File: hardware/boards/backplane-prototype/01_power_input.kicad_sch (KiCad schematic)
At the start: 42 parts, among them J5 DC INPUT (GND / +VIN), U2 LM5164DDAR, U3 LM5164DDAR, U4 INA237AIDGSR

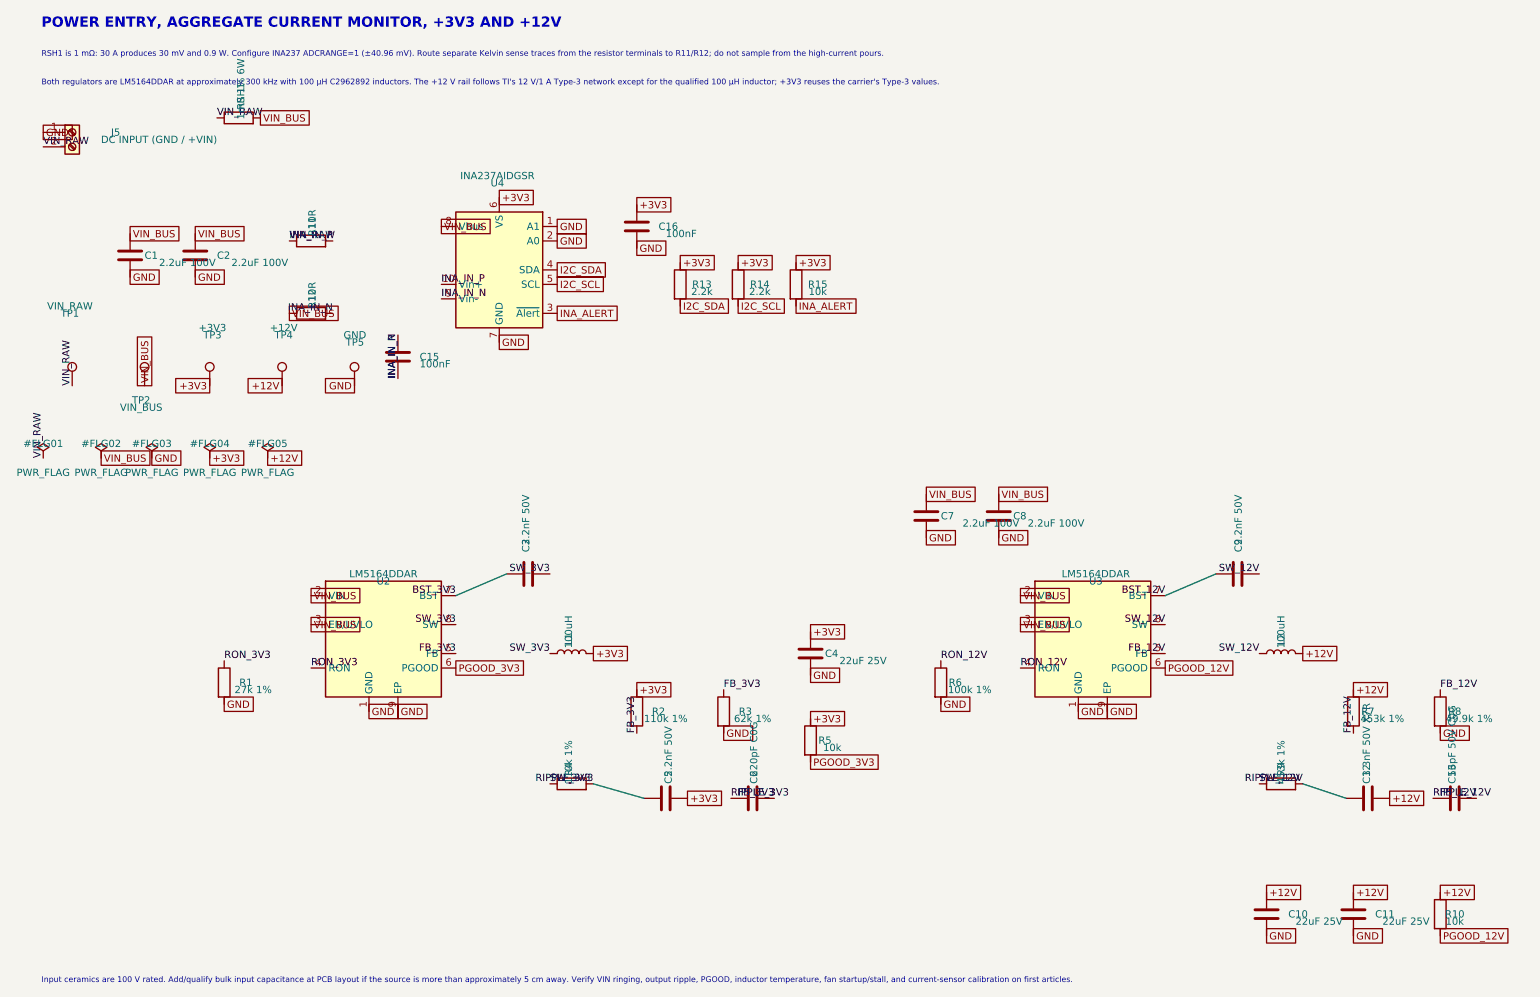
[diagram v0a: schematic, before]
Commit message: checkpoint backplane PCB synchronization
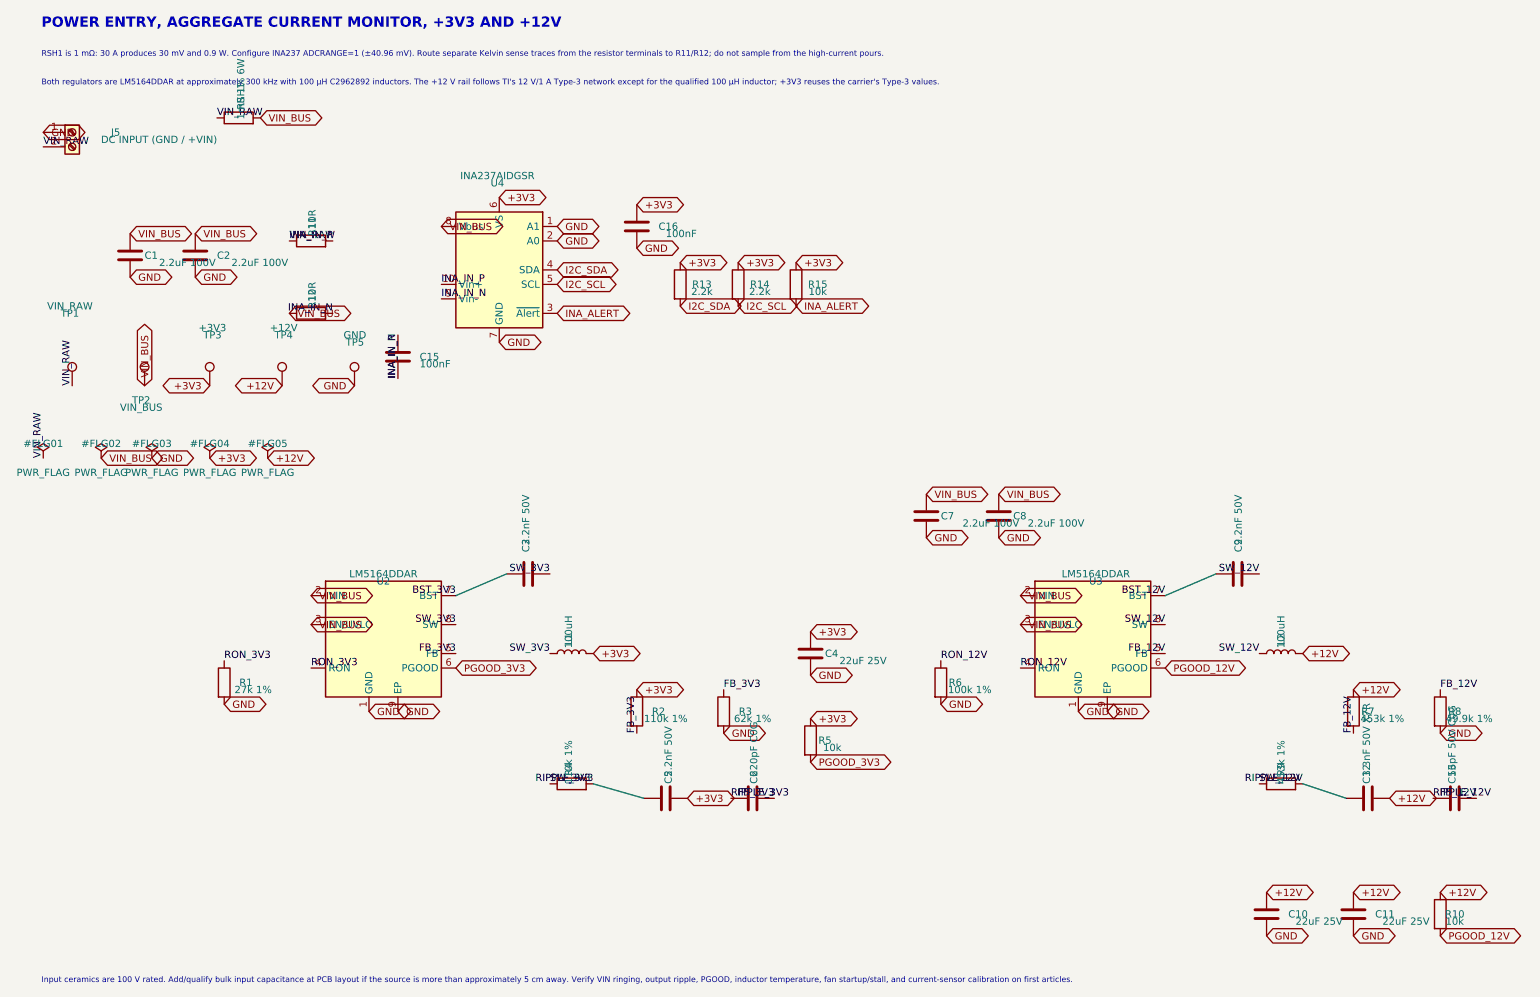
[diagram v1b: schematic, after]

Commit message: hardware: mark all test points DNP
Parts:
- TP1, TP2, TP3, TP4, TP5: now not fitted; now left out of the parts list
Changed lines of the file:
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@@
 		(body_style 1)
 		(exclude_from_sim no)
-		(in_bom yes)
+		(in_bom no)
 		(on_board yes)
 		(in_pos_files yes)
-		(dnp no)
+		(dnp yes)
 		(property "Reference" "TP2"
 			(at 37.5 82.55 0)
@@
 		(body_style 1)
 		(exclude_from_sim no)
-		(in_bom yes)
+		(in_bom no)
 		(on_board yes)
 		(in_pos_files yes)
-		(dnp no)
+		(dnp yes)
 		(property "Reference" "TP5"
 			(at 75 72.39 0)
@@
 		(body_style 1)
 		(exclude_from_sim no)
-		(in_bom yes)
+		(in_bom no)
 		(on_board yes)
 		(in_pos_files yes)
-		(dnp no)
+		(dnp yes)
 		(property "Reference" "TP1"
 			(at 25 67.31 0)
@@
 		(body_style 1)
 		(exclude_from_sim no)
-		(in_bom yes)
+		(in_bom no)
 		(on_board yes)
 		(in_pos_files yes)
-		(dnp no)
+		(dnp yes)
 		(property "Reference" "TP4"
 			(at 62.5 71.12 0)
@@
 		(body_style 1)
 		(exclude_from_sim no)
-		(in_bom yes)
+		(in_bom no)
 		(on_board yes)
 		(in_pos_files yes)
-		(dnp no)
+		(dnp yes)
 		(property "Reference" "TP3"
 			(at 50 71.12 0)

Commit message: hardware: remove unused 3v3 power-good pull-up
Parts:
- removed R5: 10k, Resistor_SMD:R_0603_1608Metric, symbol Device:R
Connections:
- net PGOOD_3V3: no longer names the net of U2.6 (PGOOD)
- no-connect marks 0 -> 1
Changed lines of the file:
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@@
 		)
 	)
-	(global_label "PGOOD_3V3"
-		(shape bidirectional)
-		(at 154.94 146.05 0)
-		(effects
-			(font
-				(size 1.27 1.27)
-			)
-			(justify left)
-		)
-		(property "Intersheetrefs" "${INTERSHEET_REFS}"
-			(at 154.94 146.05 0)
-			(hide yes)
-			(show_name no)
-			(do_not_autoplace no)
-			(effects
-				(font
-					(size 1.27 1.27)
-				)
-			)
-		)
-	)
-	(global_label "+3V3"
-		(shape bidirectional)
-		(at 154.94 138.43 0)
-		(effects
-			(font
-				(size 1.27 1.27)
-			)
-			(justify left)
-		)
-		(property "Intersheetrefs" "${INTERSHEET_REFS}"
-			(at 154.94 138.43 0)
-			(hide yes)
-			(show_name no)
-			(do_not_autoplace no)
-			(effects
-				(font
-					(size 1.27 1.27)
-				)
-			)
-		)
-	)
 	(global_label "VIN_BUS"
 		(shape bidirectional)
@@
 		)
 	)
-	(global_label "PGOOD_3V3"
-		(shape bidirectional)
-		(at 92.71 129.54 0)
-		(effects
-			(font
-				(size 1.27 1.27)
-			)
-			(justify left)
-		)
-		(property "Intersheetrefs" "${INTERSHEET_REFS}"
-			(at 92.71 129.54 0)
-			(hide yes)
-			(show_name no)
-			(do_not_autoplace no)
-			(effects
-				(font
-					(size 1.27 1.27)
-				)
-			)
-		)
-	)
 	(global_label "GND"
 		(shape bidirectional)
@@
 	)
 	(symbol
-		(lib_id "Device:R")
-		(at 154.94 142.24 0)
-		(unit 1)
-		(body_style 1)
-		(exclude_from_sim no)
-		(in_bom yes)
-		(on_board yes)
-		(in_pos_files yes)
-		(dnp no)
-		(property "Reference" "R5"
-			(at 157.48 142.24 0)
-			(show_name no)
-			(do_not_autoplace no)
-			(effects
-				(font
-					(size 1.27 1.27)
-				)
-			)
-		)
-		(property "Value" "10k"
-			(at 158.75 143.51 0)
-			(show_name no)
-			(do_not_autoplace no)
-			(effects
-				(font
-					(size 1.27 1.27)
-				)
-			)
-		)
-		(property "Footprint" "Resistor_SMD:R_0603_1608Metric"
-			(at 153.222 142.5 90)
-			(hide yes)
-			(show_name no)
-			(do_not_autoplace no)
-			(effects
-				(font
-					(size 1.27 1.27)
-				)
-			)
-		)
-		(property "Datasheet" ""
-			(at 155 142.5 0)
-			(hide yes)
-			(show_name no)
-			(do_not_autoplace no)
-			(effects
-				(font
-					(size 1.27 1.27)
-				)
-			)
-		)
-		(property "Description" ""
-			(at 155 142.5 0)
-			(hide yes)
-			(show_name no)
-			(do_not_autoplace no)
-			(effects
-				(font
-					(size 1.27 1.27)
-				)
-			)
-		)
-		(property "MPN" "0603WAF1002T5E"
-			(at 155 142.5 0)
-			(hide yes)
-			(show_name no)
-			(do_not_autoplace no)
-			(effects
-				(font
-					(size 1.27 1.27)
-				)
-			)
-		)
-		(property "Manufacturer" "UNI-ROYAL (Uniroyal Elec)"
-			(at 155 142.5 0)
-			(hide yes)
-			(show_name no)
-			(do_not_autoplace no)
-			(effects
-				(font
-					(size 1.27 1.27)
-				)
-			)
-		)
-		(property "LCSC" "C25804"
-			(at 155 142.5 0)
-			(hide yes)
-			(show_name no)
-			(do_not_autoplace no)
-			(effects
-				(font
-					(size 1.27 1.27)
-				)
-			)
-		)
-		(property "Tolerance" "1%"
-			(at 155 142.5 0)
-			(hide yes)
-			(show_name no)
-			(do_not_autoplace no)
-			(effects
-				(font
-					(size 1.27 1.27)
-				)
-			)
-		)
-		(pin "1"
-		)
-		(pin "2"
-		)
-		(instances
-			(project "backplane-prototype"
-				(path "/348cc909-6345-4013-9bef-98714057a65b/077a6190-5781-45af-8c40-d2834d2d8f2c"
-					(reference "R5")
-					(unit 1)
-				)
-			)
-		)
-	)
-	(symbol
 		(lib_id "Connector:TestPoint")
 		(at 49.53 80.01 0)
@@
 		)
 	)
+	(no_connect
+		(at 92.71 129.54)
+	)
 	(sheet_instances

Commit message: checkpoint before 12V and VCC power symbol conversion
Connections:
- net VIN_BUS: no longer C7.1
- new net VCC: C7.1

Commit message: use official 12V and VCC power symbols
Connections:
- net VIN_BUS is gone; now on net VCC: C1.1, C2.1, C8.1, R12.1, RSH1.2, TP2.1, U2.2 (VIN), U2.3 (EN/UVLO), U3.2 (VIN), U3.3 (EN/UVLO), U4.8 (Vbus)
